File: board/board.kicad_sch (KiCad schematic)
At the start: 38 parts, among them U101 Pico, U102 CS42438

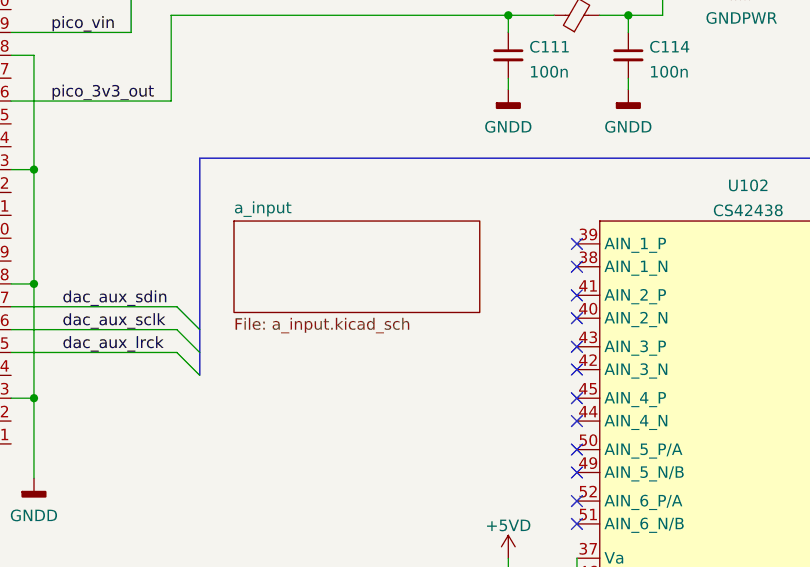
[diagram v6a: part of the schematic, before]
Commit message: some pcb digital moved
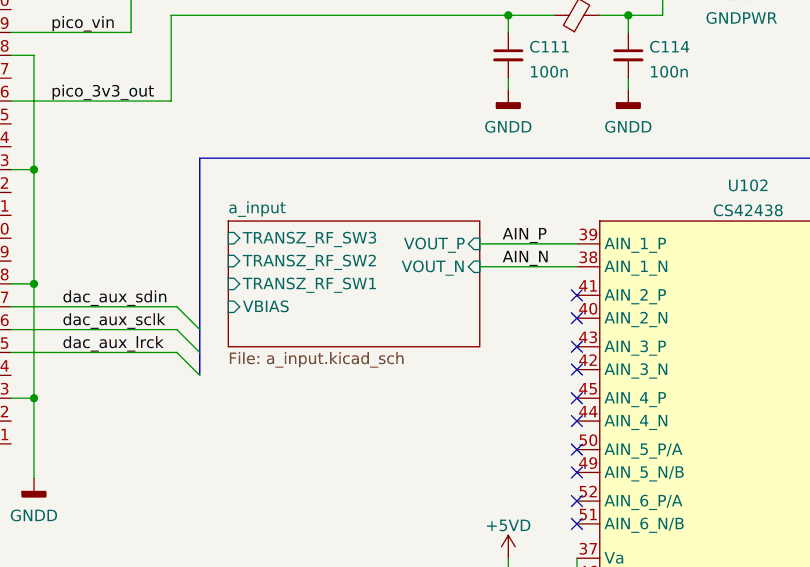
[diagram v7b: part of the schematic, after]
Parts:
- C110: footprint (none) -> Capacitor_SMD:CP_Elec_10x10
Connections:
- net AIN_N: now reaches U102.38 (AIN_1_N)
- net AIN_P: now reaches U102.39 (AIN_1_P)
- no-connect marks 24 -> 22
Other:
- sheet a_input ports: added TRANSZ_RF_SW1, TRANSZ_RF_SW2, TRANSZ_RF_SW3, VBIAS, VOUT_N, VOUT_P; removed none
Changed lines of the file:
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@@
   (no_connect (at 172.085 68.58))
   (no_connect (at 172.085 71.755))
-  (no_connect (at 172.085 57.15))
   (no_connect (at 172.085 62.865))
   (no_connect (at 172.085 60.325))
   (no_connect (at 172.085 66.04))
-  (no_connect (at 172.085 54.61))
   (no_connect (at 172.085 80.01))
   (no_connect (at 172.085 85.725))
@@
     (stroke (width 0) (type default) (color 0 0 0 0))
   )
+  (wire (pts (xy 161.29 54.61) (xy 172.085 54.61))
+    (stroke (width 0) (type default) (color 0 0 0 0))
+  )
   (wire (pts (xy 118.11 92.075) (xy 118.11 99.06))
     (stroke (width 0) (type default) (color 0 0 0 0))
@@
   )
   (wire (pts (xy 240.03 131.445) (xy 260.35 131.445))
+    (stroke (width 0) (type default) (color 0 0 0 0))
+  )
+  (wire (pts (xy 161.29 57.15) (xy 172.085 57.15))
     (stroke (width 0) (type default) (color 0 0 0 0))
   )
@@
     (effects (font (size 1.27 1.27)) (justify right bottom))
   )
+  (label "AIN_P" (at 163.83 54.61 0)
+    (effects (font (size 1.27 1.27)) (justify left bottom))
+  )
   (label "dac_ctrl_clk" (at 110.49 116.205 0)
     (effects (font (size 1.27 1.27)) (justify left bottom))
@@
   )
   (label "pico_vin" (at 113.665 31.115 0)
+    (effects (font (size 1.27 1.27)) (justify left bottom))
+  )
+  (label "AIN_N" (at 163.83 57.15 0)
     (effects (font (size 1.27 1.27)) (justify left bottom))
   )
@@
       (effects (font (size 1.27 1.27)) (justify left))
     )
-    (property "Footprint" "" (id 2) (at 158.115 101.6 0)
+    (property "Footprint" "Capacitor_SMD:CP_Elec_10x10" (id 2) (at 158.115 101.6 0)
       (effects (font (size 1.27 1.27)) hide)
     )
@@
     (pin "2")
   )
-  (sheet (at 133.985 52.07) (size 27.305 10.16) (fields_autoplaced)
+  (sheet (at 133.35 52.07) (size 27.94 13.97) (fields_autoplaced)
     (stroke (width 0.1524) (type solid) (color 0 0 0 0))
     (fill (color 0 0 0 0.0000))
-    (property "Sheet name" "a_input" (id 0) (at 133.985 51.3584 0)
+    (property "Sheet name" "a_input" (id 0) (at 133.35 51.3584 0)
       (effects (font (size 1.27 1.27)) (justify left bottom))
     )
-    (property "Sheet file" "a_input.kicad_sch" (id 1) (at 133.985 62.8146 0)
+    (property "Sheet file" "a_input.kicad_sch" (id 1) (at 133.35 66.6246 0)
       (effects (font (size 1.27 1.27)) (justify left top))
+    )
+    (pin "VBIAS" input (at 133.35 61.595 180)
+      (effects (font (size 1.27 1.27)) (justify left))
+    )
+    (pin "TRANSZ_RF_SW1" input (at 133.35 59.055 180)
+      (effects (font (size 1.27 1.27)) (justify left))
+    )
+    (pin "TRANSZ_RF_SW3" input (at 133.35 53.975 180)
+      (effects (font (size 1.27 1.27)) (justify left))
+    )
+    (pin "TRANSZ_RF_SW2" input (at 133.35 56.515 180)
+      (effects (font (size 1.27 1.27)) (justify left))
+    )
+    (pin "VOUT_P" input (at 161.29 54.61 0)
+      (effects (font (size 1.27 1.27)) (justify right))
+    )
+    (pin "VOUT_N" input (at 161.29 57.15 0)
+      (effects (font (size 1.27 1.27)) (justify right))
     )
   )
@@
     )
     (path "/fe6fae53-576d-4efc-98a4-3f3b0adbefd1"
-      (reference "C110") (unit 1) (value "330u") (footprint "")
+      (reference "C110") (unit 1) (value "330u") (footprint "Capacitor_SMD:CP_Elec_10x10")
     )
     (path "/93017893-f580-4a2b-8868-c7786292fa8c"
@@
     )
     (path "/7b9c2940-9a15-4fc8-9338-3451987ef45d/230120dd-d473-409d-bc85-a303aaf0db58"
-      (reference "C201") (unit 1) (value "330u") (footprint "")
+      (reference "C201") (unit 1) (value "330u") (footprint "Capacitor_SMD:CP_Elec_10x10")
     )
     (path "/7b9c2940-9a15-4fc8-9338-3451987ef45d/76c0f64e-d771-4598-9b70-c8bf4629cc50"
@@
     )
     (path "/f559c6b4-e02e-46c0-aefe-18fd627650bc/d8ee1488-fc88-4fe1-9359-5cbe390e6c3e"
-      (reference "C308") (unit 1) (value "100n") (footprint "Capacitor_SMD:C_0603_1608Metric_Pad1.08x0.95mm_HandSolder")
+      (reference "C308") (unit 1) (value "100p") (footprint "Capacitor_SMD:C_0603_1608Metric_Pad1.08x0.95mm_HandSolder")
     )
     (path "/8c7f8209-e8bf-40a6-8c80-26f603dd71db/02d7daeb-3293-45c5-8b0e-1c9b1755cd8a"
@@
     )
     (path "/8c7f8209-e8bf-40a6-8c80-26f603dd71db/d8ee1488-fc88-4fe1-9359-5cbe390e6c3e"
-      (reference "C408") (unit 1) (value "100n") (footprint "Capacitor_SMD:C_0603_1608Metric_Pad1.08x0.95mm_HandSolder")
+      (reference "C408") (unit 1) (value "100p") (footprint "Capacitor_SMD:C_0603_1608Metric_Pad1.08x0.95mm_HandSolder")
     )
     (path "/78b4b35c-c2e7-4bd1-bf45-979e95720873/56db283f-240b-4ee4-b5aa-7ffd7364bd0c"

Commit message: do the gng
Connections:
- net +5VD: no longer C101.1, C102.1, C103.1, C104.1, C105.1, C106.1, C108.1, C110.1, C113.1, U102.36 (Vq), U102.37 (Va), U102.46 (Va), U102.47 (FILT+)
- net AIN_N: now also U102.39 (AIN_1_P); no longer U102.38 (AIN_1_N)
- net AIN_P: now also U102.38 (AIN_1_N); no longer U102.39 (AIN_1_P)
- net a_input/VBIAS: now also C106.1, C108.1, U102.36 (Vq)
- new net +5VA: C101.1, C102.1, C103.1, C104.1, C105.1, U102.37 (Va), U102.46 (Va)
- new net vfilt: C110.1, C113.1, U102.47 (FILT+)
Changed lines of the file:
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@@
   (junction (at 155.575 147.955) (diameter 0) (color 0 0 0 0)
   )
-  (junction (at 162.56 94.615) (diameter 0) (color 0 0 0 0)
-  )
   (junction (at 134.62 106.68) (diameter 0) (color 0 0 0 0)
   )
@@
   (junction (at 111.76 46.355) (diameter 0) (color 0 0 0 0)
   )
-  (junction (at 160.655 97.155) (diameter 0) (color 0 0 0 0)
-  )
   (junction (at 170.18 109.22) (diameter 0) (color 0 0 0 0)
   )
@@
   (junction (at 150.495 94.615) (diameter 0) (color 0 0 0 0)
   )
-  (junction (at 160.655 94.615) (diameter 0) (color 0 0 0 0)
-  )
-  (junction (at 162.56 92.075) (diameter 0) (color 0 0 0 0)
-  )
   (junction (at 134.62 92.075) (diameter 0) (color 0 0 0 0)
   )
@@
   )
   (junction (at 71.12 71.755) (diameter 0) (color 0 0 0 0)
+  )
+  (junction (at 158.115 94.615) (diameter 0) (color 0 0 0 0)
   )
   (junction (at 170.815 147.955) (diameter 0) (color 0 0 0 0)
@@
     (stroke (width 0) (type default) (color 0 0 0 0))
   )
+  (wire (pts (xy 161.29 54.61) (xy 170.18 54.61))
+    (stroke (width 0) (type default) (color 0 0 0 0))
+  )
   (bus (pts (xy 37.465 64.135) (xy 37.465 159.385))
     (stroke (width 0) (type default) (color 0 0 0 0))
   )
+  (wire (pts (xy 132.08 61.595) (xy 132.08 87.63))
+    (stroke (width 0) (type default) (color 0 0 0 0))
+  )
   (wire (pts (xy 146.685 145.415) (xy 146.685 147.955))
     (stroke (width 0) (type default) (color 0 0 0 0))
@@
     (stroke (width 0) (type default) (color 0 0 0 0))
   )
+  (wire (pts (xy 168.275 55.88) (xy 171.45 55.88))
+    (stroke (width 0) (type default) (color 0 0 0 0))
+  )
   (wire (pts (xy 134.62 92.075) (xy 134.62 99.06))
     (stroke (width 0) (type default) (color 0 0 0 0))
@@
     (stroke (width 0) (type default) (color 0 0 0 0))
   )
-  (wire (pts (xy 162.56 92.075) (xy 162.56 94.615))
-    (stroke (width 0) (type default) (color 0 0 0 0))
-  )
   (wire (pts (xy 122.555 26.67) (xy 122.555 31.115))
     (stroke (width 0) (type default) (color 0 0 0 0))
@@
     (stroke (width 0) (type default) (color 0 0 0 0))
   )
+  (wire (pts (xy 168.275 57.15) (xy 168.275 55.88))
+    (stroke (width 0) (type default) (color 0 0 0 0))
+  )
   (wire (pts (xy 210.185 133.985) (xy 232.41 133.985))
     (stroke (width 0) (type default) (color 0 0 0 0))
@@
     (stroke (width 0) (type default) (color 0 0 0 0))
   )
-  (wire (pts (xy 160.655 94.615) (xy 160.655 97.155))
-    (stroke (width 0) (type default) (color 0 0 0 0))
-  )
   (bus (pts (xy 37.465 51.435) (xy 37.465 53.975))
     (stroke (width 0) (type default) (color 0 0 0 0))
@@
     (stroke (width 0) (type default) (color 0 0 0 0))
   )
+  (wire (pts (xy 170.18 57.15) (xy 172.085 57.15))
+    (stroke (width 0) (type default) (color 0 0 0 0))
+  )
   (wire (pts (xy 170.18 106.68) (xy 170.18 109.22))
     (stroke (width 0) (type default) (color 0 0 0 0))
@@
     (stroke (width 0) (type default) (color 0 0 0 0))
   )
-  (wire (pts (xy 161.29 54.61) (xy 172.085 54.61))
-    (stroke (width 0) (type default) (color 0 0 0 0))
-  )
   (wire (pts (xy 118.11 92.075) (xy 118.11 99.06))
     (stroke (width 0) (type default) (color 0 0 0 0))
   )
-  (wire (pts (xy 162.56 92.075) (xy 134.62 92.075))
-    (stroke (width 0) (type default) (color 0 0 0 0))
-  )
   (wire (pts (xy 164.465 36.195) (xy 164.465 37.465))
     (stroke (width 0) (type default) (color 0 0 0 0))
@@
     (stroke (width 0) (type default) (color 0 0 0 0))
   )
+  (wire (pts (xy 133.35 61.595) (xy 132.08 61.595))
+    (stroke (width 0) (type default) (color 0 0 0 0))
+  )
   (wire (pts (xy 71.12 59.055) (xy 73.66 59.055))
     (stroke (width 0) (type default) (color 0 0 0 0))
@@
     (stroke (width 0) (type default) (color 0 0 0 0))
   )
-  (wire (pts (xy 160.655 97.155) (xy 158.115 97.155))
-    (stroke (width 0) (type default) (color 0 0 0 0))
-  )
   (wire (pts (xy 210.185 60.325) (xy 222.25 60.325))
     (stroke (width 0) (type default) (color 0 0 0 0))
@@
     (stroke (width 0) (type default) (color 0 0 0 0))
   )
+  (wire (pts (xy 170.18 54.61) (xy 170.18 57.15))
+    (stroke (width 0) (type default) (color 0 0 0 0))
+  )
   (wire (pts (xy 71.12 71.755) (xy 71.12 80.645))
     (stroke (width 0) (type default) (color 0 0 0 0))
@@
     (stroke (width 0) (type default) (color 0 0 0 0))
   )
-  (wire (pts (xy 160.655 94.615) (xy 150.495 94.615))
+  (wire (pts (xy 150.495 94.615) (xy 158.115 94.615))
     (stroke (width 0) (type default) (color 0 0 0 0))
   )
@@
     (stroke (width 0) (type default) (color 0 0 0 0))
   )
-  (wire (pts (xy 164.465 92.075) (xy 162.56 92.075))
+  (wire (pts (xy 134.62 92.075) (xy 164.465 92.075))
     (stroke (width 0) (type default) (color 0 0 0 0))
   )
@@
     (stroke (width 0) (type default) (color 0 0 0 0))
   )
+  (wire (pts (xy 158.115 87.63) (xy 158.115 94.615))
+    (stroke (width 0) (type default) (color 0 0 0 0))
+  )
   (bus (pts (xy 104.14 123.825) (xy 104.14 126.365))
     (stroke (width 0) (type default) (color 0 0 0 0))
@@
     (stroke (width 0) (type default) (color 0 0 0 0))
   )
+  (wire (pts (xy 161.29 57.15) (xy 168.275 57.15))
+    (stroke (width 0) (type default) (color 0 0 0 0))
+  )
   (wire (pts (xy 158.115 97.155) (xy 158.115 99.06))
     (stroke (width 0) (type default) (color 0 0 0 0))
@@
     (stroke (width 0) (type default) (color 0 0 0 0))
   )
+  (wire (pts (xy 171.45 54.61) (xy 172.085 54.61))
+    (stroke (width 0) (type default) (color 0 0 0 0))
+  )
   (wire (pts (xy 51.435 74.295) (xy 73.66 74.295))
     (stroke (width 0) (type default) (color 0 0 0 0))
@@
     (stroke (width 0) (type default) (color 0 0 0 0))
   )
-  (wire (pts (xy 166.37 97.155) (xy 160.655 97.155))
+  (wire (pts (xy 158.115 97.155) (xy 166.37 97.155))
     (stroke (width 0) (type default) (color 0 0 0 0))
   )
@@
     (stroke (width 0) (type default) (color 0 0 0 0))
   )
+  (wire (pts (xy 171.45 55.88) (xy 171.45 54.61))
+    (stroke (width 0) (type default) (color 0 0 0 0))
+  )
   (wire (pts (xy 109.22 64.135) (xy 127.635 64.135))
     (stroke (width 0) (type default) (color 0 0 0 0))
@@
     (stroke (width 0) (type default) (color 0 0 0 0))
   )
-  (wire (pts (xy 161.29 57.15) (xy 172.085 57.15))
+  (wire (pts (xy 158.115 94.615) (xy 172.085 94.615))
     (stroke (width 0) (type default) (color 0 0 0 0))
   )
@@
     (stroke (width 0) (type default) (color 0 0 0 0))
   )
+  (wire (pts (xy 132.08 87.63) (xy 158.115 87.63))
+    (stroke (width 0) (type default) (color 0 0 0 0))
+  )
   (wire (pts (xy 240.03 118.745) (xy 281.94 118.745))
     (stroke (width 0) (type default) (color 0 0 0 0))
@@
     (stroke (width 0) (type default) (color 0 0 0 0))
   )
-  (wire (pts (xy 162.56 94.615) (xy 160.655 94.615))
-    (stroke (width 0) (type default) (color 0 0 0 0))
-  )
   (wire (pts (xy 127 29.21) (xy 164.465 29.21))
     (stroke (width 0) (type default) (color 0 0 0 0))
@@
   )
   (wire (pts (xy 106.68 116.205) (xy 125.73 116.205))
-    (stroke (width 0) (type default) (color 0 0 0 0))
-  )
-  (wire (pts (xy 172.085 94.615) (xy 162.56 94.615))
     (stroke (width 0) (type default) (color 0 0 0 0))
   )
@@
   )
   (label "AIN_P" (at 163.83 54.61 0)
+    (effects (font (size 1.27 1.27)) (justify left bottom))
+  )
+  (label "vfilt" (at 161.925 97.155 0)
     (effects (font (size 1.27 1.27)) (justify left bottom))
   )
@@
     (pin "2")
   )
-  (symbol (lib_id "power:+5VD") (at 164.465 89.535 0) (unit 1)
-    (in_bom yes) (on_board yes) (fields_autoplaced)
-    (property "Reference" "#PWR0106" (id 0) (at 164.465 93.345 0)
-      (effects (font (size 1.27 1.27)) hide)
-    )
-    (property "Value" "+5VD" (id 1) (at 164.465 85.9305 0))
-    (property "Footprint" "" (id 2) (at 164.465 89.535 0)
-      (effects (font (size 1.27 1.27)) hide)
-    )
-    (property "Datasheet" "" (id 3) (at 164.465 89.535 0)
-      (effects (font (size 1.27 1.27)) hide)
-    )
-    (pin "1")
-  )
   (symbol (lib_id "power:+3V3") (at 170.815 135.255 0) (unit 1)
     (in_bom yes) (on_board yes) (fields_autoplaced)
@@
     (pin "1")
     (pin "2")
+  )
+  (symbol (lib_id "power:+5VA") (at 164.465 89.535 0) (unit 1)
+    (in_bom yes) (on_board yes) (fields_autoplaced)
+    (property "Reference" "#PWR0106" (id 0) (at 164.465 93.345 0)
+      (effects (font (size 1.27 1.27)) hide)
+    )
+    (property "Value" "+5VA" (id 1) (at 164.465 85.9305 0))
+    (property "Footprint" "" (id 2) (at 164.465 89.535 0)
+      (effects (font (size 1.27 1.27)) hide)
+    )
+    (property "Datasheet" "" (id 3) (at 164.465 89.535 0)
+      (effects (font (size 1.27 1.27)) hide)
+    )
+    (pin "1")
   )
   (symbol (lib_id "Device:R") (at 236.22 116.205 90) (unit 1)
@@
       (reference "#PWR0105") (unit 1) (value "GNDD") (footprint "")
     )
-    (path "/3dc6dcd1-c36d-43e2-a3ff-e37dcf21ac24"
-      (reference "#PWR0106") (unit 1) (value "+5VD") (footprint "")
+    (path "/e8be1274-9bdd-4e35-b974-d055106fcd6c"
+      (reference "#PWR0106") (unit 1) (value "+5VA") (footprint "")
     )
     (path "/e0c5b036-6e91-4391-a29c-13796620b2c1"
